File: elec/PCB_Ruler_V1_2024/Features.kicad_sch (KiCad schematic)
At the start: 12 parts, among them U4 TCA9534PWR, U5 VL53L4CXV0DH/1

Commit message: Hi handsome :)
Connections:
- net +3.3V: now also MT1.1 (AP_SDO/AP_AD0), MT1.12 (AP_CS)
- net GND: now also MT1.7 (FSYNC)
- net INT1_IMU: now reaches MT1.4 (INT1/INT)
- net INT2_IMU: now reaches MT1.9 (INT2)
- no-connect marks 2 -> 6
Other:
- note added: "ADRESSE: 0X52"
- note added: "ADRESSE: 0X64"
- note added: "ADRESSE: 0X69"

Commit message: started the pcb
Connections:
- net AVDD is gone; now on net +3.3V: C10.1, C11.1, U5.1 (AVDDVCSEL), U5.11 (AVDD)
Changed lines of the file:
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@@
 		)
 	)
-	(global_label "AVDD"
+	(global_label "XSHUT"
 		(shape input)
-		(at 157.48 132.08 90)
+		(at 243.84 54.61 180)
 		(fields_autoplaced yes)
 		(effects
@@
 				(size 1.27 1.27)
 			)
-			(justify left)
+			(justify right)
 		)
 		(property "Intersheetrefs" "${INTERSHEET_REFS}"
-			(at 157.48 124.3776 90)
-			(effects
-				(font
-					(size 1.27 1.27)
-				)
-				(justify left)
-				(hide yes)
-			)
-		)
-	)
-	(global_label "XSHUT"
+			(at 234.8072 54.61 0)
+			(effects
+				(font
+					(size 1.27 1.27)
+				)
+				(justify right)
+				(hide yes)
+			)
+		)
+	)
+	(global_label "INT_IO_Extender"
 		(shape input)
-		(at 243.84 54.61 180)
+		(at 209.55 102.87 180)
 		(fields_autoplaced yes)
 		(effects
@@
 		)
 		(property "Intersheetrefs" "${INTERSHEET_REFS}"
-			(at 234.8072 54.61 0)
+			(at 191.6272 102.87 0)
 			(effects
 				(font
@@
 		)
 	)
-	(global_label "INT_IO_Extender"
+	(global_label "XSHUT"
 		(shape input)
-		(at 209.55 102.87 180)
+		(at 38.1 146.05 180)
 		(fields_autoplaced yes)
 		(effects
@@
 		)
 		(property "Intersheetrefs" "${INTERSHEET_REFS}"
-			(at 191.6272 102.87 0)
+			(at 29.0672 146.05 0)
 			(effects
 				(font
@@
 		)
 	)
-	(global_label "XSHUT"
+	(global_label "Button2"
 		(shape input)
-		(at 38.1 146.05 180)
+		(at 247.65 107.95 0)
 		(fields_autoplaced yes)
 		(effects
@@
 				(size 1.27 1.27)
 			)
-			(justify right)
+			(justify left)
 		)
 		(property "Intersheetrefs" "${INTERSHEET_REFS}"
-			(at 29.0672 146.05 0)
-			(effects
-				(font
-					(size 1.27 1.27)
-				)
-				(justify right)
-				(hide yes)
-			)
-		)
-	)
-	(global_label "Button2"
+			(at 258.0131 107.95 0)
+			(effects
+				(font
+					(size 1.27 1.27)
+				)
+				(justify left)
+				(hide yes)
+			)
+		)
+	)
+	(global_label "SCL"
 		(shape input)
-		(at 247.65 107.95 0)
+		(at 96.52 140.97 0)
 		(fields_autoplaced yes)
 		(effects
@@
 		)
 		(property "Intersheetrefs" "${INTERSHEET_REFS}"
-			(at 258.0131 107.95 0)
+			(at 103.0128 140.97 0)
 			(effects
 				(font
@@
 		)
 	)
-	(global_label "SCL"
+	(global_label "IO7"
 		(shape input)
-		(at 96.52 140.97 0)
+		(at 247.65 118.11 0)
 		(fields_autoplaced yes)
 		(effects
@@
 		)
 		(property "Intersheetrefs" "${INTERSHEET_REFS}"
-			(at 103.0128 140.97 0)
+			(at 253.78 118.11 0)
 			(effects
 				(font
@@
 		)
 	)
-	(global_label "IO7"
+	(global_label "SDA"
 		(shape input)
-		(at 247.65 118.11 0)
+		(at 27.94 68.58 180)
 		(fields_autoplaced yes)
 		(effects
@@
 				(size 1.27 1.27)
 			)
-			(justify left)
+			(justify right)
 		)
 		(property "Intersheetrefs" "${INTERSHEET_REFS}"
-			(at 253.78 118.11 0)
-			(effects
-				(font
-					(size 1.27 1.27)
-				)
-				(justify left)
-				(hide yes)
-			)
-		)
-	)
-	(global_label "SDA"
+			(at 21.3867 68.58 0)
+			(effects
+				(font
+					(size 1.27 1.27)
+				)
+				(justify right)
+				(hide yes)
+			)
+		)
+	)
+	(global_label "XSHUT"
 		(shape input)
-		(at 27.94 68.58 180)
+		(at 247.65 102.87 0)
 		(fields_autoplaced yes)
 		(effects
@@
 				(size 1.27 1.27)
 			)
-			(justify right)
+			(justify left)
 		)
 		(property "Intersheetrefs" "${INTERSHEET_REFS}"
-			(at 21.3867 68.58 0)
-			(effects
-				(font
-					(size 1.27 1.27)
-				)
-				(justify right)
-				(hide yes)
-			)
-		)
-	)
-	(global_label "XSHUT"
+			(at 256.6828 102.87 0)
+			(effects
+				(font
+					(size 1.27 1.27)
+				)
+				(justify left)
+				(hide yes)
+			)
+		)
+	)
+	(global_label "Button3"
 		(shape input)
-		(at 247.65 102.87 0)
+		(at 247.65 110.49 0)
 		(fields_autoplaced yes)
 		(effects
@@
 		)
 		(property "Intersheetrefs" "${INTERSHEET_REFS}"
-			(at 256.6828 102.87 0)
+			(at 258.0131 110.49 0)
 			(effects
 				(font
@@
 		)
 	)
-	(global_label "Button3"
+	(global_label "SCL"
 		(shape input)
-		(at 247.65 110.49 0)
+		(at 27.94 66.04 180)
 		(fields_autoplaced yes)
 		(effects
@@
 				(size 1.27 1.27)
 			)
-			(justify left)
+			(justify right)
 		)
 		(property "Intersheetrefs" "${INTERSHEET_REFS}"
-			(at 258.0131 110.49 0)
-			(effects
-				(font
-					(size 1.27 1.27)
-				)
-				(justify left)
-				(hide yes)
-			)
-		)
-	)
-	(global_label "SCL"
+			(at 21.4472 66.04 0)
+			(effects
+				(font
+					(size 1.27 1.27)
+				)
+				(justify right)
+				(hide yes)
+			)
+		)
+	)
+	(global_label "AVDDVCSEL"
 		(shape input)
-		(at 27.94 66.04 180)
+		(at 38.1 135.89 180)
 		(fields_autoplaced yes)
 		(effects
@@
 		)
 		(property "Intersheetrefs" "${INTERSHEET_REFS}"
-			(at 21.4472 66.04 0)
+			(at 24.6524 135.89 0)
 			(effects
 				(font
@@
 		)
 	)
-	(global_label "AVDDVCSEL"
+	(global_label "SCL"
 		(shape input)
-		(at 38.1 135.89 180)
+		(at 209.55 105.41 180)
 		(fields_autoplaced yes)
 		(effects
@@
 		)
 		(property "Intersheetrefs" "${INTERSHEET_REFS}"
-			(at 24.6524 135.89 0)
+			(at 203.0572 105.41 0)
 			(effects
 				(font
@@
 	(global_label "SCL"
 		(shape input)
-		(at 209.55 105.41 180)
+		(at 223.52 54.61 180)
 		(fields_autoplaced yes)
 		(effects
@@
 		)
 		(property "Intersheetrefs" "${INTERSHEET_REFS}"
-			(at 203.0572 105.41 0)
-			(effects
-				(font
-					(size 1.27 1.27)
-				)
-				(justify right)
-				(hide yes)
-			)
-		)
-	)
-	(global_label "SCL"
-		(shape input)
-		(at 223.52 54.61 180)
-		(fields_autoplaced yes)
-		(effects
-			(font
-				(size 1.27 1.27)
-			)
-			(justify right)
-		)
-		(property "Intersheetrefs" "${INTERSHEET_REFS}"
 			(at 217.0272 54.61 0)
 			(effects
@@
 					(unit 1)
 				)
+			)
+		)
+	)
+	(symbol
+		(lib_id "power:+3.3V")
+		(at 157.48 132.08 0)
+		(unit 1)
+		(exclude_from_sim no)
+		(in_bom yes)
+		(on_board yes)
+		(dnp no)
+		(fields_autoplaced yes)
+		(property "Reference" "#PWR019"
+			(at 157.48 135.89 0)
+			(effects
+				(font
+					(size 1.27 1.27)
+				)
+				(hide yes)
+			)
+		)
+		(property "Value" "+3.3V"
+			(at 157.48 127 0)
+			(effects
+				(font
+					(size 1.27 1.27)
+				)
+			)
+		)
+		(property "Footprint" ""
+			(at 157.48 132.08 0)
+			(effects
+				(font
+					(size 1.27 1.27)
+				)
+				(hide yes)
+			)
+		)
+		(property "Datasheet" ""
+			(at 157.48 132.08 0)
+			(effects
+				(font
+					(size 1.27 1.27)
+				)
+				(hide yes)
+			)
+		)
+		(property "Description" "Power symbol creates a global label with name \"+3.3V\""
+			(at 157.48 132.08 0)
+			(effects
+				(font
+					(size 1.27 1.27)
+				)
+				(hide yes)
+			)
+		)
+		(pin "1"
+		)
+		(instances
+			(project "PCB_Ruler_V1_2024"
+				(path "/e39575e5-bba1-47dc-9ccf-32a84e6da237/ca7d0597-655a-4aee-bb72-0094cc7418df"
+					(reference "#PWR019")
+					(unit 1)
+				)

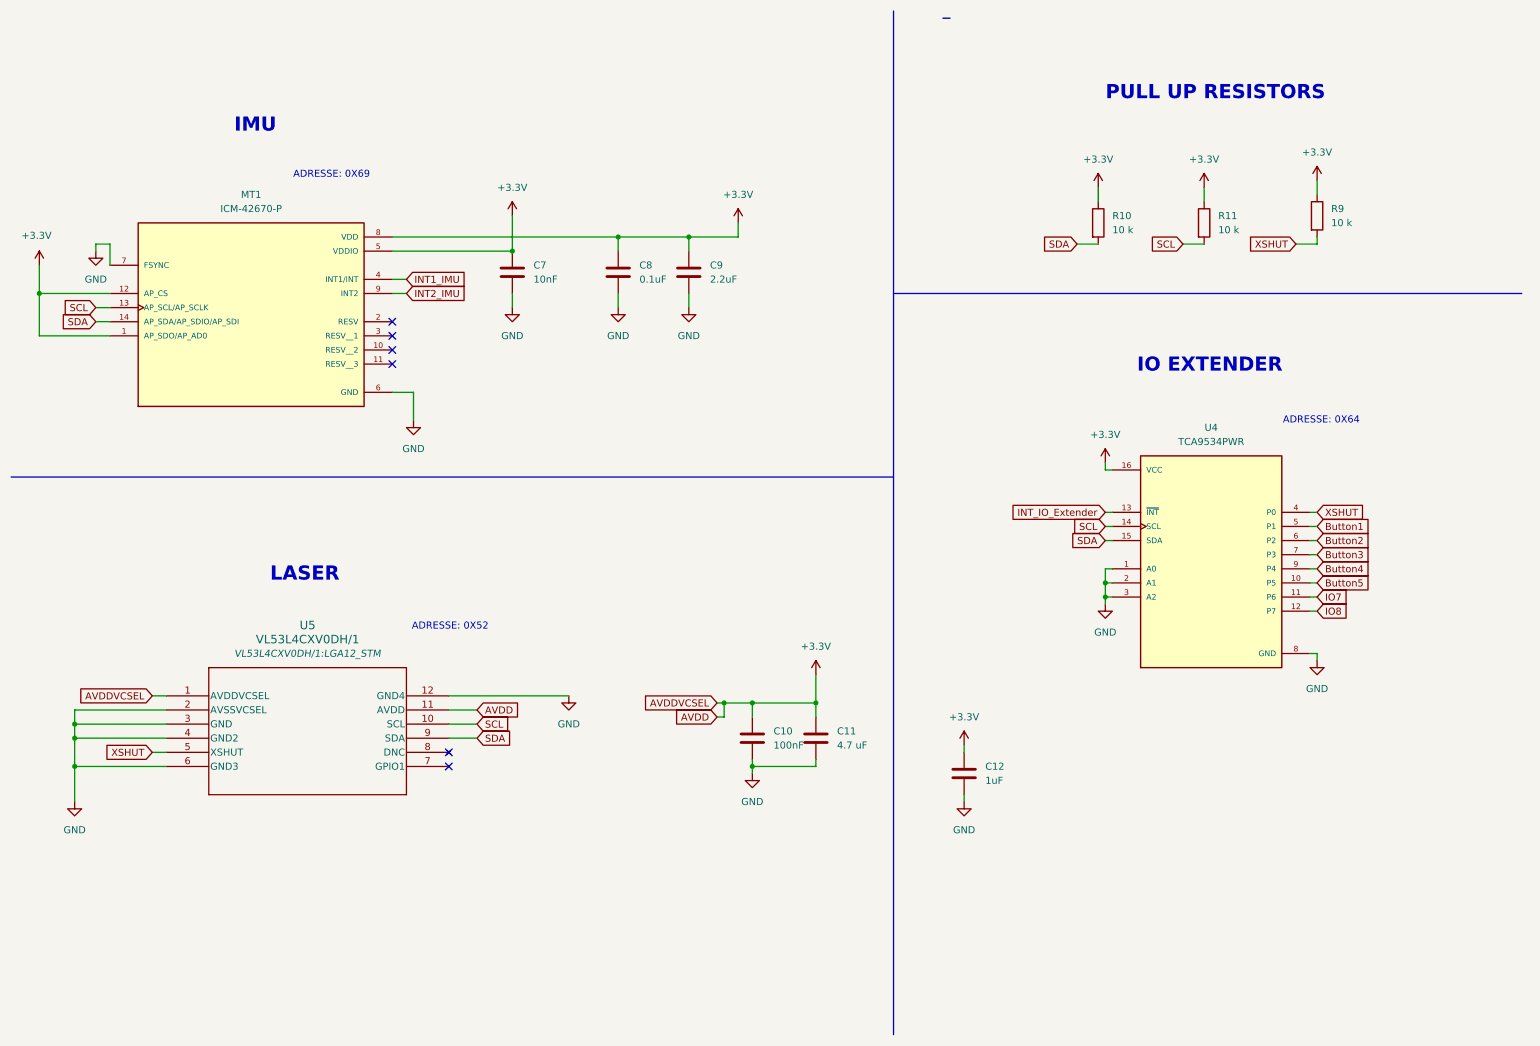
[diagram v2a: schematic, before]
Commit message: Added to schematic what was missing
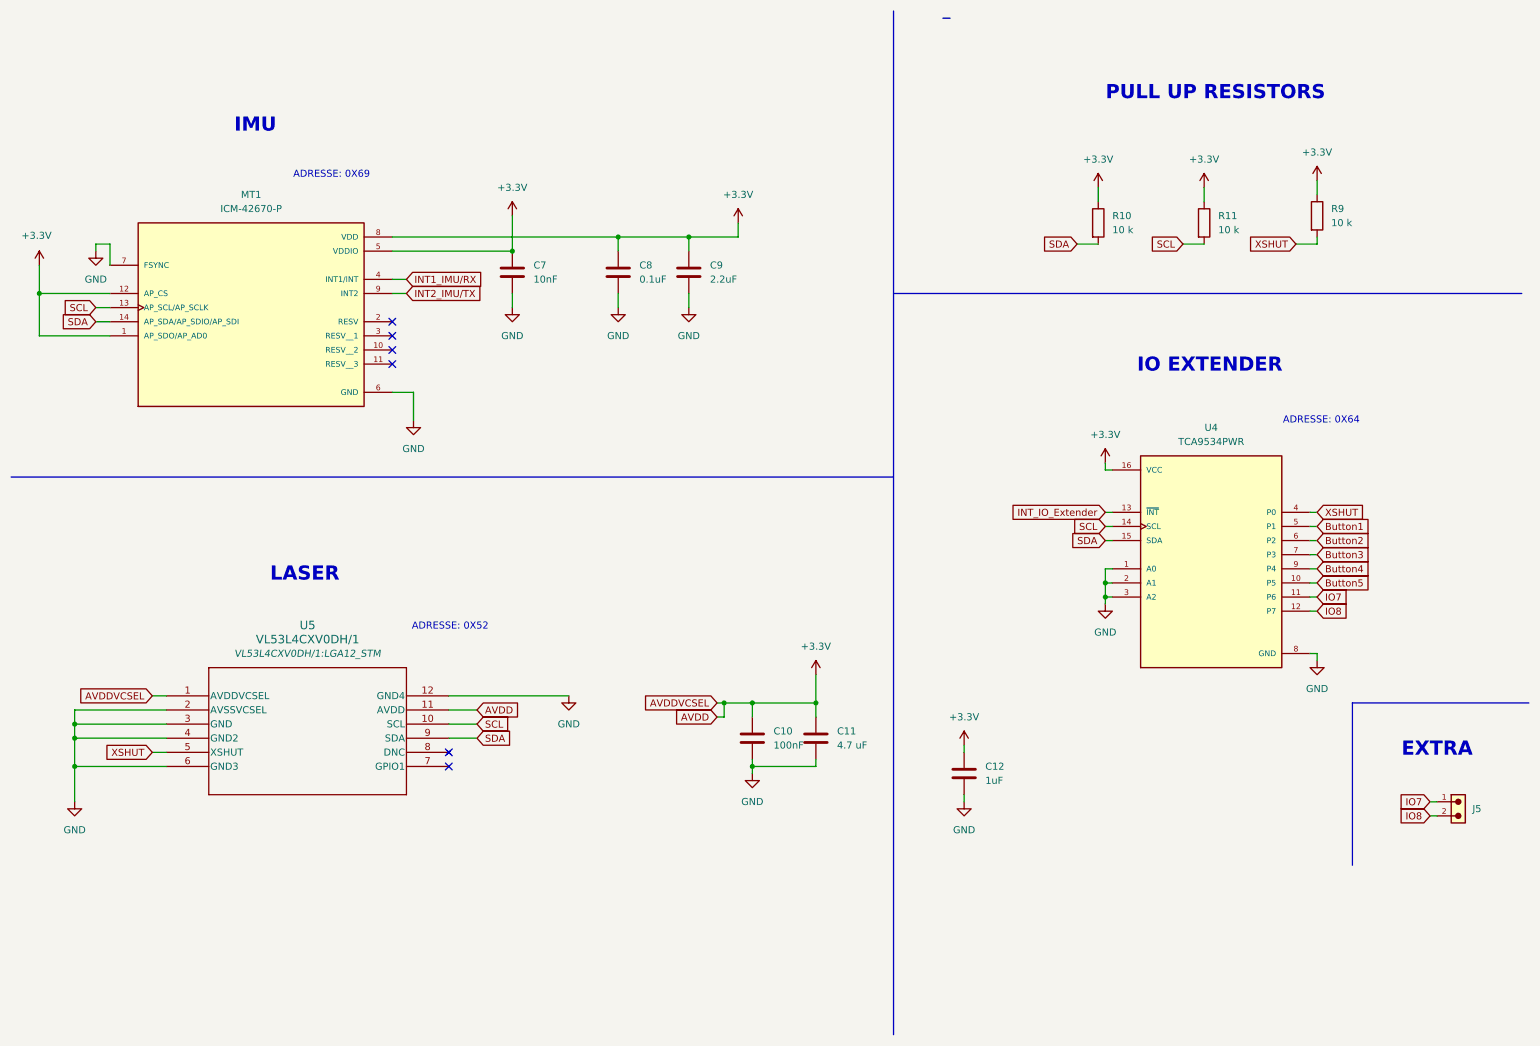
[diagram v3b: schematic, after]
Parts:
- added J5: 61300211121, Header2_1:61300211121, symbol Header2_1:6130XX11121_61300211121
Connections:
- net IO7: now also J5.1
- net IO8: now also J5.2
- net INT1_IMU renamed INT1_IMU/RX
- net INT2_IMU renamed INT2_IMU/TX
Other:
- note added: "EXTRA"

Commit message: coucou v2
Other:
- note added: "ADRESSE: 0X20"
- note removed: "ADRESSE: 0X64"
- company: (none) -> FRANK_LAU
- title: (none) -> FONCTIONNALITÉS_RULER 2024
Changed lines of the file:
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@@
 	(generator_version "8.0")
 	(paper "A4")
+	(title_block
+		(title "FONCTIONNALITÉS_RULER 2024")
+		(date "2024-12-27")
+		(rev "B")
+		(company "FRANK_LAU")
+	)
 	(junction
 		(at 209.55 115.57)
@@
 		)
 	)
-	(text "ADRESSE: 0X64"
+	(text "ADRESSE: 0X20"
 		(exclude_from_sim no)
 		(at 248.412 86.36 0)
